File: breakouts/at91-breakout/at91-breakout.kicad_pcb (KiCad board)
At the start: 4 copper layers, 137.2 x 43.2 mm, 42 parts, among them J1 UART0, J10 MemCtl, J11 ~INSTRD, J12 ~WAIT, J13 ~BUSREQACK, J14 IRQ, J14 ~NMI, J15 JTAG, J16 TRIGOUT, J17 PHI, J18 UART1, J19 VDD, J2 TIMER, J20 RTC_VDD, J21 GND, J22 TTY, J3 ADDR[0..23], J4 I2C, J4 ~WDOVF, J5 GPIO, J5 RTC_XINOUT, J6 CLKINOUT, J7 ~RESET, J8 DATA[0..15], J9 ~CS[0..3], U1 AT91R40008, U1 EZ80L92AZ050SG, U2 BB Powered, U3 PC Powered

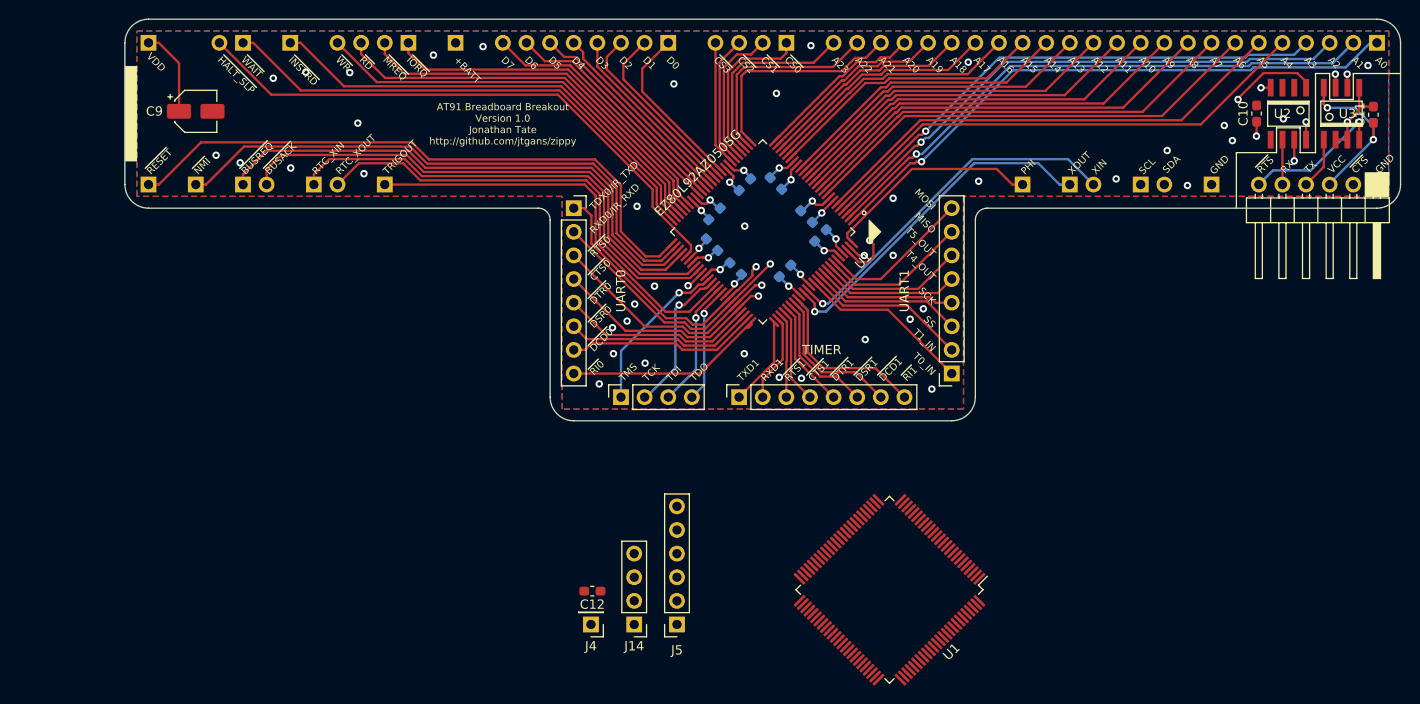
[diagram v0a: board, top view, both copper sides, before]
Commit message: Finished routing the AT91 breakout board
May want to reroute later. It wasn't the best job.
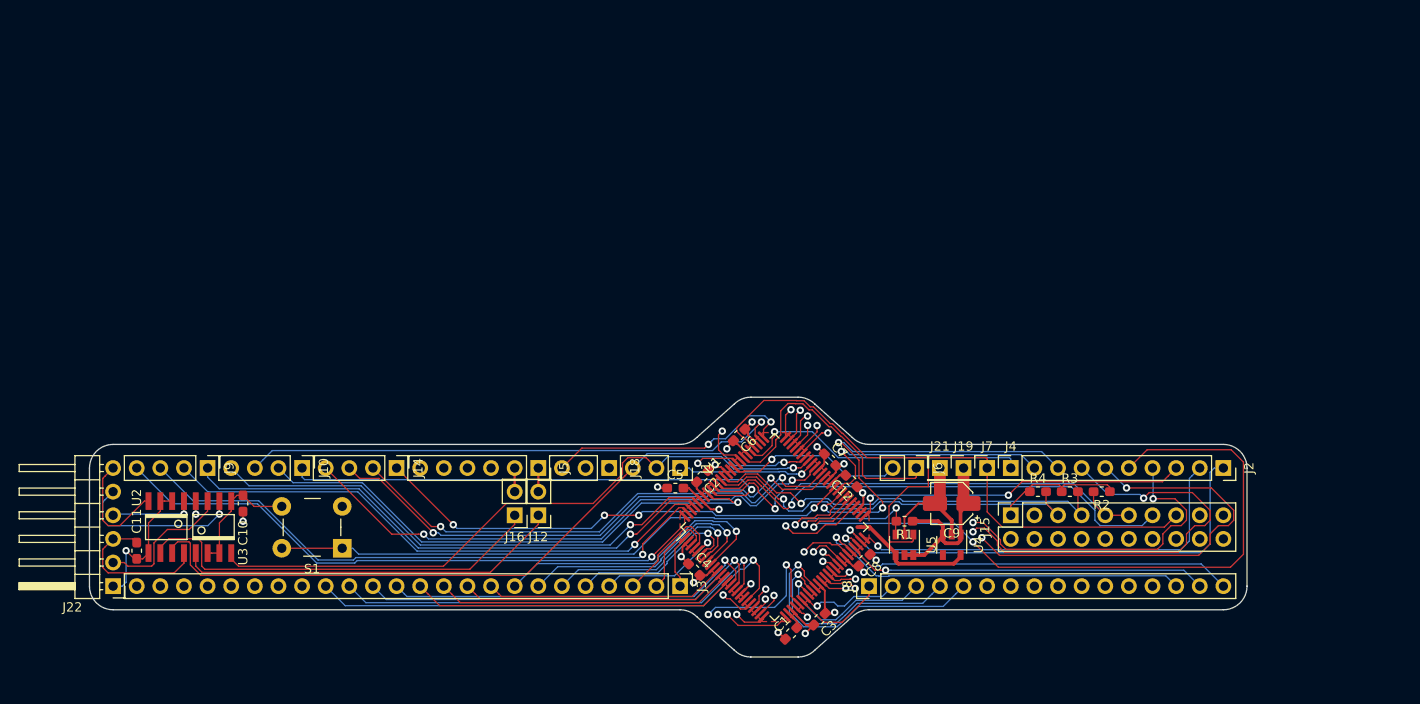
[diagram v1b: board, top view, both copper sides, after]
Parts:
- removed G***: LOGO, footprints:oshw_small
- removed J11: ~INSTRD, Connector_PinHeader_2.54mm:PinHeader_1x01_P2.54mm_Vertical
- removed J13: ~BUSREQACK, Connector_PinHeader_2.54mm:PinHeader_1x02_P2.54mm_Vertical
- removed the J14 at (133.5, 115.9)
- removed the J14 at (86.4, 68.6)
- removed J17: PHI, Connector_PinHeader_2.54mm:PinHeader_1x01_P2.54mm_Vertical
- removed J20: RTC_VDD, Connector_PinHeader_2.54mm:PinHeader_1x01_P2.54mm_Vertical
- removed the J4 at (128.8, 115.9)
- removed the J4 at (188.0, 68.6)
- removed the J5 at (138.1, 115.9)
- removed the J5 at (99.1, 68.6)
- removed the U1 at (160.9, 112.2)
- removed the U1 at (147.3, 73.7)
- added J14: IRQ, Connector_PinHeader_2.54mm:PinHeader_1x04_P2.54mm_Vertical, F.Cu at (108.0, 99.1)
- added J4: ~WDOVF, Connector_PinHeader_2.54mm:PinHeader_1x01_P2.54mm_Vertical, F.Cu at (174.0, 99.1)
- added J5: GPIO, Connector_PinSocket_2.54mm:PinSocket_1x06_P2.54mm_Vertical, F.Cu at (123.2, 99.1)
- added R1: 100K, Resistor_SMD:R_0603_1608Metric_Pad1.05x0.95mm_HandSolder, F.Cu at (162.6, 104.8)
- added R2: 100K, Resistor_SMD:R_0603_1608Metric_Pad1.05x0.95mm_HandSolder, F.Cu at (183.8, 101.6)
- added R3: 100K, Resistor_SMD:R_0603_1608Metric_Pad1.05x0.95mm_HandSolder, F.Cu at (180.3, 101.6)
- added R4: 100K, Resistor_SMD:R_0603_1608Metric_Pad1.05x0.95mm_HandSolder, F.Cu at (176.9, 101.6)
- added S1: B3F-1000, digikey-footprints:Switch_Tactile_THT_B3F-1xxx, F.Cu at (102.1, 107.7)
- added U1: AT91R40008, Package_QFP:LQFP-100_14x14mm_P0.5mm, F.Cu at (148.6, 105.4)
- added U4: MIC5504-1.8YM5, Package_TO_SOT_SMD:SOT-23-5, F.Cu at (167.6, 107.3)
- added U5: MAX6355TW, Package_TO_SOT_SMD:SOT-23-6, F.Cu at (162.6, 107.3)
- C1, C2, C3, C4, C5, C6, C7, C8, J19, J21, J3, J6, J7, J9: moved to F.Cu
- J1, J18: footprint Connector_PinSocket_2.54mm:PinSocket_1x08_P2.54mm_Vertical -> Connector_PinSocket_2.54mm:PinSocket_1x03_P2.54mm_Vertical
- J10: value MemCtl -> BUSCTL; moved to F.Cu
- J12: value ~WAIT -> RTSCB0; moved to F.Cu
- J15: footprint Connector_PinSocket_2.54mm:PinSocket_1x04_P2.54mm_Vertical -> Connector_PinSocket_2.54mm:PinSocket_2x10_P2.54mm_Vertical
- J16: value TRIGOUT -> CTSCB0; footprint Connector_PinHeader_2.54mm:PinHeader_1x01_P2.54mm_Vertical -> Connector_PinHeader_2.54mm:PinHeader_1x02_P2.54mm_Vertical; moved to F.Cu
- J2: footprint Connector_PinSocket_2.54mm:PinSocket_1x08_P2.54mm_Vertical -> Connector_PinSocket_2.54mm:PinSocket_1x09_P2.54mm_Vertical
- J8: footprint Connector_PinHeader_2.54mm:PinHeader_1x08_P2.54mm_Vertical -> Connector_PinHeader_2.54mm:PinHeader_1x16_P2.54mm_Vertical; moved to F.Cu
- moved J22 142.6 mm to (77.5, 111.8), turned to 180 degrees
- moved C11 141.0 mm to (80.0, 108.0), turned to -90 degrees
- moved U3 134.0 mm to (83.2, 105.4), turned to 180 degrees
- moved U2 123.8 mm to (88.3, 105.4), turned to 0 degrees
- moved C10 116.8 mm to (91.4, 102.9)
- moved J19 98.8 mm to (168.9, 99.1), turned to 0 degrees
- moved J7 95.2 mm to (171.4, 99.1), turned to 0 degrees
- moved J3 95.0 mm to (138.4, 111.8), turned to -90 degrees
- moved C9 91.6 mm to (167.6, 102.9), turned to 180 degrees
- moved J9 77.2 mm to (87.6, 99.1), turned to -90 degrees
- moved J8 62.3 mm to (158.8, 111.8)
- moved J12 59.9 mm to (123.2, 104.1), turned to 180 degrees
- moved J2 52.6 mm to (196.8, 99.1), turned to -90 degrees
- moved C1 48.4 mm to (150.4, 116.8), turned to 45 degrees
- moved J10 47.1 mm to (97.8, 99.1), turned to -90 degrees
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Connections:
- net /FTDI_TX0 renamed /FTDI_TX
- net /FTDI_TX1 renamed /~FTDI_RTS
- net /RX0 renamed /RXD0
- C1 pad 2: +3V3 -> +1V8
- C12 pad 2: +3V3 -> +1V8
- C2 pad 2: +3V3 -> +1V8
- C6 pad 2: +1V8 -> +3V3
- C7 pad 2: +1V8 -> +3V3
- C8 pad 2: +1V8 -> +3V3
- J1 pad 2: /TX0 -> /TXD0
- J12 pad 1: /~WAIT -> /~RTS0
- J12 pad 2: /~HALT_SLP -> /P16
- J15 pad 1: /TMS -> +3V3
- J15 pad 2: /TDI -> +3V3
- J15 pad 3: /TDO -> Net-(J15-Pad3)
- J15 pad 4: /TCK -> GND
- J16 pad 1: /TRIGOUT -> /~CTS0
- J18 pad 2: /TX1 -> /TXD1
- J18 pad 3: /RX1 -> /RXD1
- J22 pad 2: /FTDI_RX1 -> /~FTDI_CTS
- J22 pad 5: /FTDI_RX0 -> /FTDI_RX
- U2 pad 1: /TX0 -> /~RTS0
- U2 pad 4: /TX1 -> /TXD0
- U2 pad 6: /FTDI_RX1 -> /FTDI_RX
- U2 pad 7: /FTDI_RX0 -> /~FTDI_CTS
- U3 pad 6: /RX1 -> /~CTS0
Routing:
- net /PD3: track 101.2 -> 0.00 mm
- net /PD1: track 100.3 -> 0.00 mm
- net /PD2: track 98.9 -> 0.00 mm
- net /PD0: track 94.5 -> 0.00 mm
- net /RXD0: track 0.00 -> 78.2 mm, vias 2 -> 1
- net /TIOA1: track 0.00 -> 77.6 mm, vias 0 -> 2
- net /TIOB1: track 0.00 -> 73.9 mm, vias 0 -> 3
- net /TCLK2: track 0.00 -> 73.2 mm, vias 0 -> 3
- net /~MR: track 0.00 -> 71.4 mm, vias 0 -> 1
- net /TXD0: track 0.00 -> 70.5 mm, vias 0 -> 1
- net /TCLK1: track 0.00 -> 65.1 mm, vias 0 -> 3
- net /~HALT_SLP: track 62.2 -> 0.00 mm
- net /~NMI: track 61.9 -> 0.00 mm
- net /FIQ: track 0.00 -> 60.0 mm, vias 0 -> 2
- net /ADDR23: track 20.9 -> 80.0 mm, vias 0 -> 2
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- added copper zone on F.Cu, net +1V8
- added copper zone on In1.Cu, net +3V3
- added copper zone on In2.Cu, net GND
- removed copper zone on In2.Cu, net +3V3
- removed copper zone on B.Cu, net GND
- removed copper zone on F.Cu, net GND
- removed copper zone on In1.Cu, net GND
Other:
- board size 137.2 x 43.2 mm -> 124.5 x 27.9 mm
- net class Default: clearance 0.2 -> 0.127; trace_width 0.25 -> 0.127
- rule trace_clearance: 0.2 -> 0.127
- rule trace_min: 0.2 -> 0.127
- rule via_min_drill: 0.3 -> 0.254
- rule via_min_size: 0.4 -> 0.3556
- board text removed: "+BATT"
- board text removed: "A0"
- board text removed: "A1"
- board text removed: "A10"
- board text removed: "A11"
- board text removed: "A12"
- board text removed: "A13"
- board text removed: "A14"
- board text removed: "A15"
- board text removed: "A16"
- board text removed: "A17"
- board text removed: "A18"
- board text removed: "A19"
- board text removed: "A2"
- board text removed: "A20"
- board text removed: "A21"
- board text removed: "A22"
- board text removed: "A23"
- board text removed: "A3"
- board text removed: "A4"
- board text removed: "A5"
- board text removed: "A6"
- board text removed: "A7"
- board text removed: "A8"
- board text removed: "A9"
- board text removed: "AT91 Breadboard Breakout Version 1.0 Jonathan Tate http://github.com/jtgans/zippy"
- board text removed: "D0"
- board text removed: "D1"
- board text removed: "D2"
- board text removed: "D3"
- board text removed: "D4"
- board text removed: "D5"
- board text removed: "D6"
- board text removed: "D7"
- board text removed: "GND"
- board text removed: "MISO"
- board text removed: "MOSI"
- board text removed: "PHI"
- board text removed: "RTC_XIN"
- board text removed: "RTC_XOUT"
- board text removed: "RX"
- board text removed: "RXD0/IR_RXD"
- board text removed: "RXD1"
- board text removed: "SCK"
- board text removed: "SCL"
- board text removed: "SDA"
- board text removed: "SS"
- board text removed: "T0_IN"
- board text removed: "T1_IN"
- board text removed: "T4_OUT"
- board text removed: "T5_OUT"
- board text removed: "TCK"
- board text removed: "TDI"
- board text removed: "TDO"
- board text removed: "TDX0/IR_TXD"
- board text removed: "TMS"
- board text removed: "TRIGOUT"
- board text removed: "TX"
- board text removed: "TXD1"
- board text removed: "VCC"
- board text removed: "XIN"
- board text removed: "XOUT"
- board text removed: "~BUSACK"
- board text removed: "~BUSREQ"
- board text removed: "~CS0"
- board text removed: "~CS1"
- board text removed: "~CS2"
- board text removed: "~CS3"
- board text removed: "~CTS"
- board text removed: "~CTS0"
- board text removed: "~CTS1"
- board text removed: "~DCD0"
- board text removed: "~DCD1"
- board text removed: "~DSR0"
- board text removed: "~DSR1"
- board text removed: "~DTR0"
- board text removed: "~DTR1"
- board text removed: "~HALT_SLP"
- board text removed: "~INSTRD"
- board text removed: "~IORQ"
- board text removed: "~MREQ"
- board text removed: "~NMI"
- board text removed: "~RD"
- board text removed: "~RESET"
- board text removed: "~RI0"
- board text removed: "~RI1"
- board text removed: "~RTS"
- board text removed: "~RTS0"
- board text removed: "~RTS1"
- board text removed: "~WAIT"
- board text removed: "~WR"

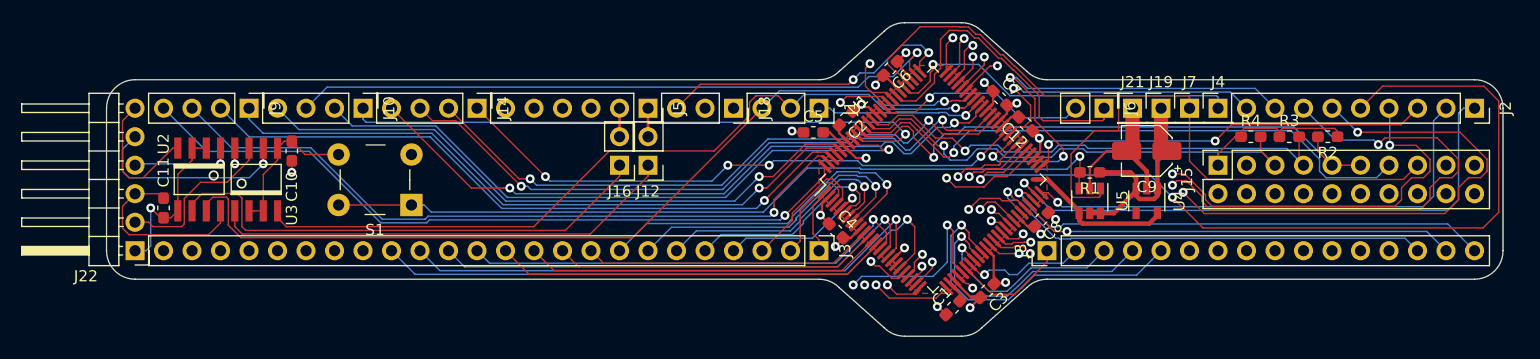
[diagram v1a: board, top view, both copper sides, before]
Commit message: Adding silkscreen labels for pins on AT91 breakout board.
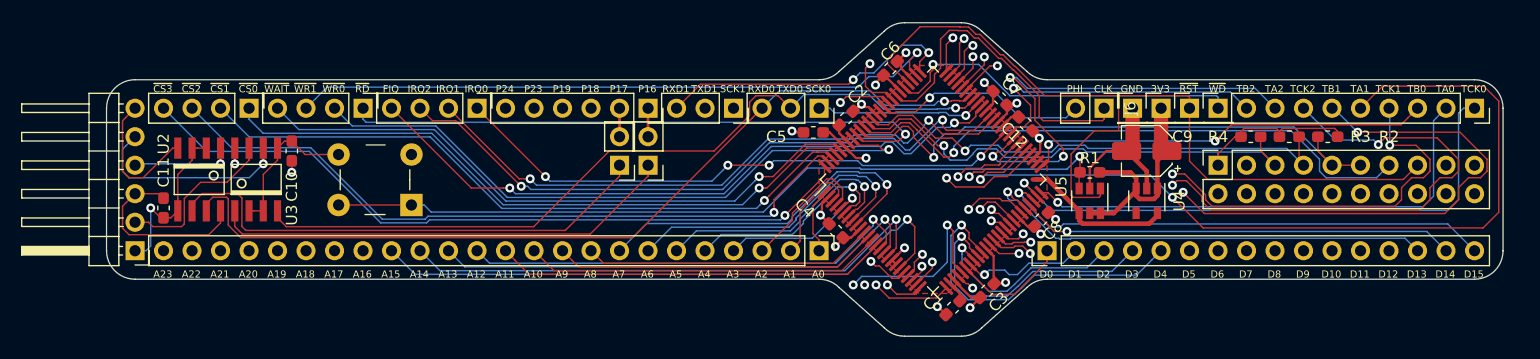
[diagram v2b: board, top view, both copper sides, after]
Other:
- board text added: "3V3"
- board text added: "A0"
- board text added: "A1"
- board text added: "A10"
- board text added: "A11"
- board text added: "A12"
- board text added: "A13"
- board text added: "A14"
- board text added: "A15"
- board text added: "A16"
- board text added: "A17"
- board text added: "A18"
- board text added: "A19"
- board text added: "A2"
- board text added: "A20"
- board text added: "A21"
- board text added: "A22"
- board text added: "A23"
- board text added: "A3"
- board text added: "A4"
- board text added: "A5"
- board text added: "A6"
- board text added: "A7"
- board text added: "A8"
- board text added: "A9"
- board text added: "CLK"
- board text added: "D0"
- board text added: "D1"
- board text added: "D10"
- board text added: "D11"
- board text added: "D12"
- board text added: "D13"
- board text added: "D14"
- board text added: "D15"
- board text added: "D2"
- board text added: "D3"
- board text added: "D4"
- board text added: "D5"
- board text added: "D6"
- board text added: "D7"
- board text added: "D8"
- board text added: "D9"
- board text added: "FIQ"
- board text added: "GND"
- board text added: "IRQ0"
- board text added: "IRQ1"
- board text added: "IRQ2"
- board text added: "P16"
- board text added: "P17"
- board text added: "P18"
- board text added: "P19"
- board text added: "P23"
- board text added: "P24"
- board text added: "PHI"
- board text added: "RXD0"
- board text added: "RXD1"
- board text added: "SCK0"
- board text added: "SCK1"
- board text added: "TA0"
- board text added: "TA1"
- board text added: "TA2"
- board text added: "TB0"
- board text added: "TB1"
- board text added: "TB2"
- board text added: "TCK0"
- board text added: "TCK1"
- board text added: "TCK2"
- board text added: "TXD0"
- board text added: "TXD1"
- board text added: "~CS0"
- board text added: "~CS1"
- board text added: "~CS2"
- board text added: "~CS3"
- board text added: "~RD"
- board text added: "~RST"
- board text added: "~WAIT"
- board text added: "~WD"
- board text added: "~WR0"
- board text added: "~WR1"
